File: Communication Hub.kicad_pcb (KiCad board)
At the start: 2 copper layers, 150 x 80 mm, 50 parts, among them J1 USB_B, J2 USB_A, J3 Conn_01x03, J4 Conn_01x02, J5 RJ45, J6 RJ45, J7 RJ45, U1 USBLC6-2SC6, U2 AT24CS02-SSHM, U3 USB2514B_Bi, U4 USBLC6-2SC6, U5 CP2102N-Axx-xQFN28, U6 MAX3485, Y1 24Mhz

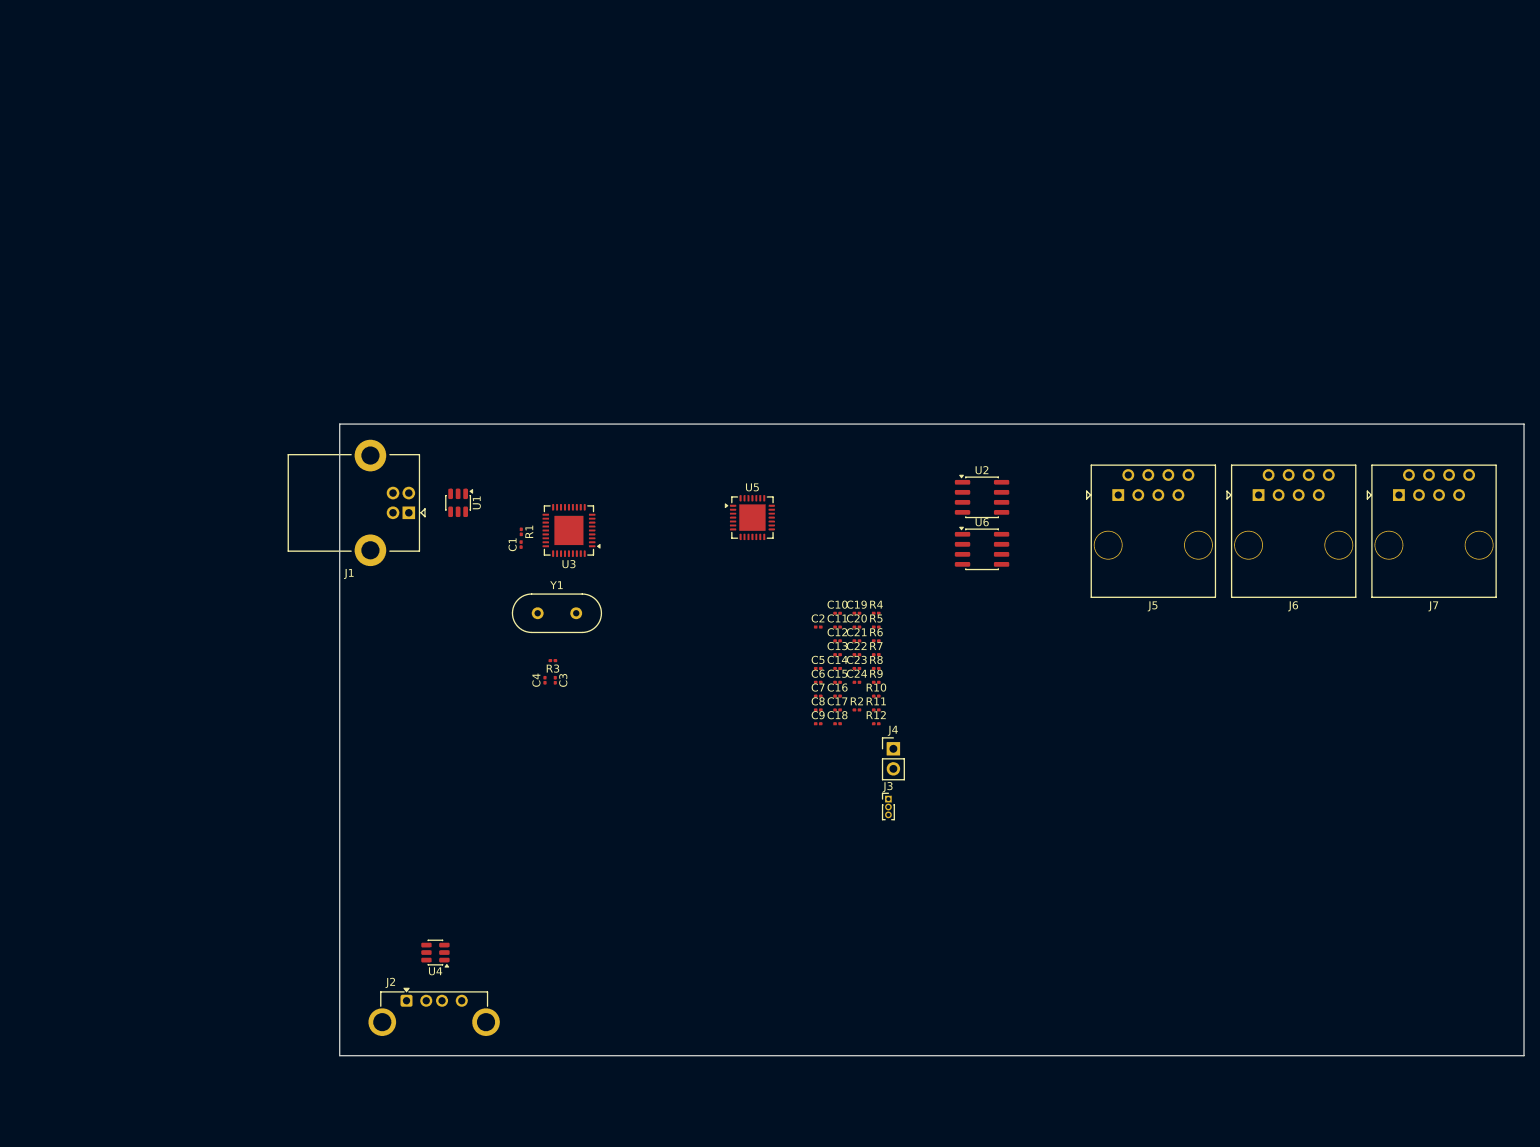
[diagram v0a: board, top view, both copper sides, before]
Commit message: Updates to schematics and pcb
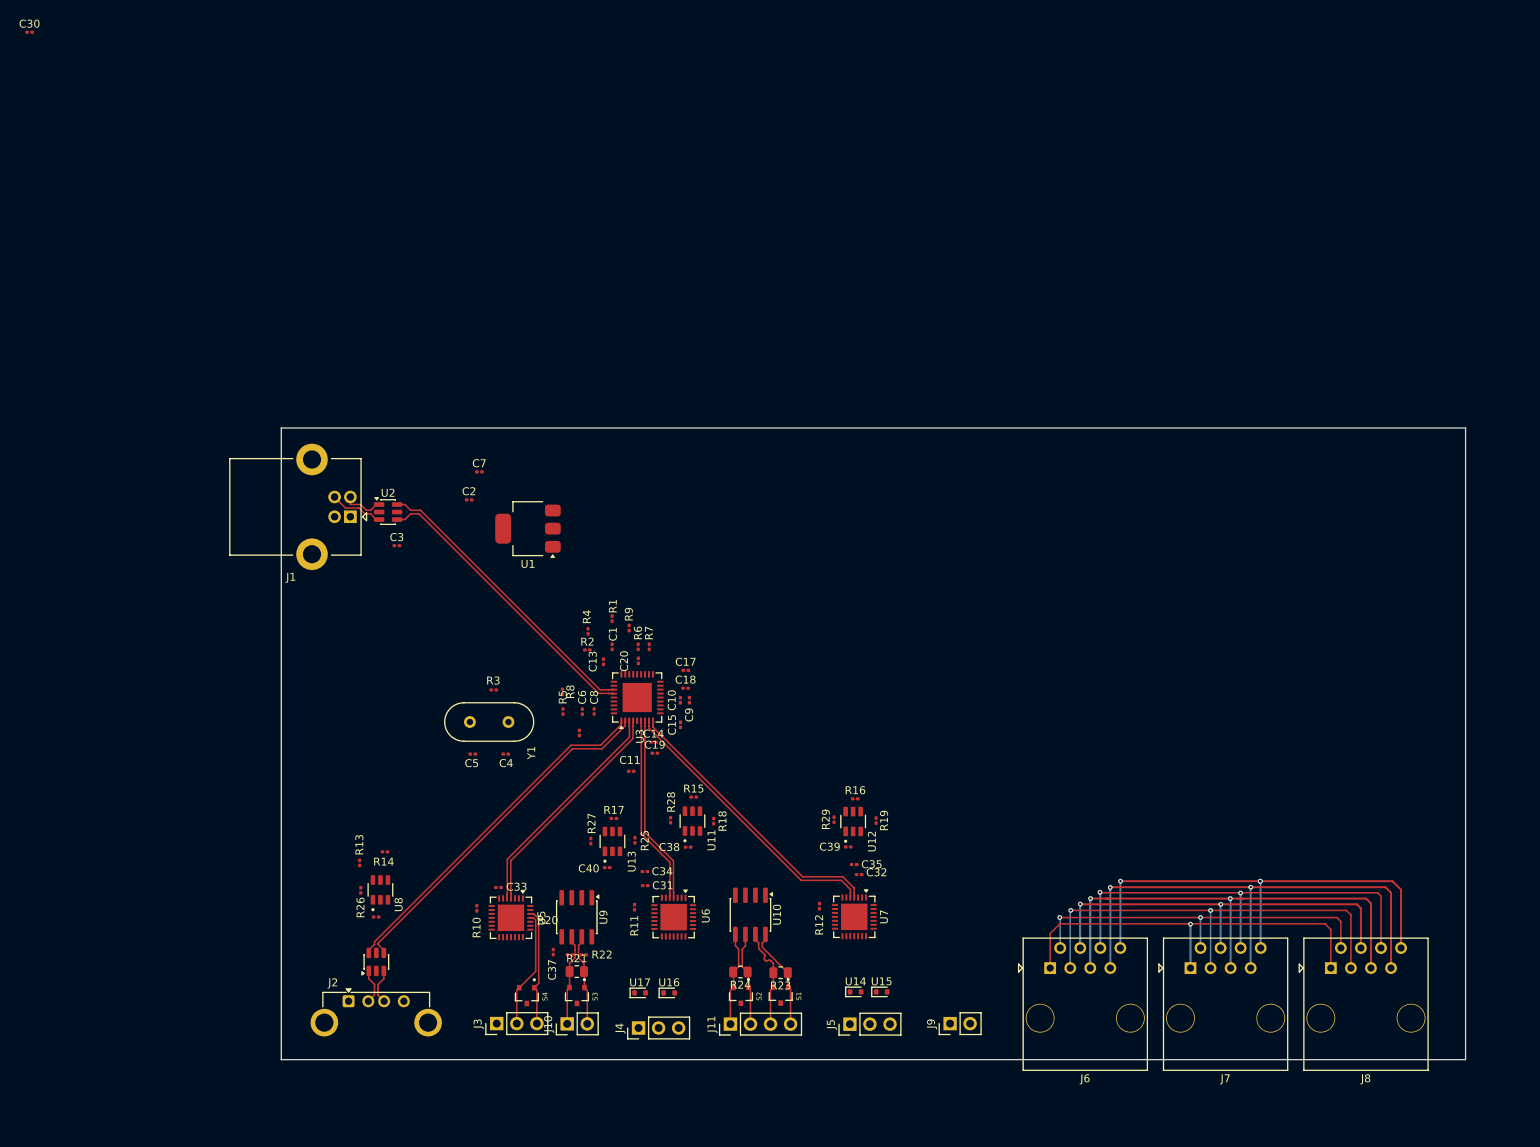
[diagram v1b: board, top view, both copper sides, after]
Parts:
- removed the C10 at (103.1, 74.0)
- removed the C19 at (105.5, 74.0)
- removed the C20 at (105.5, 75.7)
- removed C21, C22: 0,1uF, Capacitor_SMD:C_0201_0603Metric
- removed the R9 at (108.0, 82.7)
- removed the U2 at (121.4, 59.3)
- added C2: 10uF, Capacitor_SMD:C_0201_0603Metric, F.Cu at (56.4, 59.6)
- added C30: 0,1uF, Capacitor_SMD:C_0201_0603Metric, F.Cu at (0.72, 0.38)
- added C31: 0,1uF, Capacitor_SMD:C_0201_0603Metric, F.Cu at (78.7, 108.5)
- added C32: 0,1uF, Capacitor_SMD:C_0201_0603Metric, F.Cu at (105.8, 107.1)
- added C34: 4,7uF, Capacitor_SMD:C_0201_0603Metric, F.Cu at (78.7, 106.7)
- added C35: 4,7uF, Capacitor_SMD:C_0201_0603Metric, F.Cu at (105.2, 105.8)
- added C36: 0,1uF, Capacitor_SMD:C_0201_0603Metric, F.Cu at (44.6, 112.4)
- added C38: 0,1uF, Capacitor_SMD:C_0201_0603Metric, F.Cu at (84.1, 103.6)
- added C39: 0,1uF, Capacitor_SMD:C_0201_0603Metric, F.Cu at (104.4, 103.6)
- added C40: 0,1uF, Capacitor_SMD:C_0201_0603Metric, F.Cu at (73.9, 106.2)
- added C7: 22uF, Capacitor_SMD:C_0201_0603Metric, F.Cu at (57.7, 56.0)
- added J11: RS422, Connector_PinHeader_2.54mm:PinHeader_1x04_P2.54mm_Vertical, F.Cu at (89.5, 126.0)
- added J4: U6 TX RX, Connector_PinHeader_2.54mm:PinHeader_1x03_P2.54mm_Vertical, F.Cu at (77.9, 126.5)
- added J5: U7 TX RX, Connector_PinHeader_2.54mm:PinHeader_1x03_P2.54mm_Vertical, F.Cu at (104.6, 126.0)
- added J9: CAN, Connector_PinHeader_2.54mm:PinHeader_1x02_P2.54mm_Vertical, F.Cu at (117.3, 125.9)
- added R11: 10k, Resistor_SMD:R_0201_0603Metric, F.Cu at (77.3, 111.2)
- added R12: 10k, Resistor_SMD:R_0201_0603Metric, F.Cu at (100.8, 111.1)
- added R13: 49k, Resistor_SMD:R_0201_0603Metric, F.Cu at (42.5, 105.6)
- added R14: 100k, Resistor_SMD:R_0201_0603Metric, F.Cu at (45.7, 104.2)
- added R15: 235k, Resistor_SMD:R_0201_0603Metric, F.Cu at (84.8, 97.3)
- added R16: 235k, Resistor_SMD:R_0201_0603Metric, F.Cu at (105.3, 97.5)
- added R17: 235k, Resistor_SMD:R_0201_0603Metric, F.Cu at (74.7, 100.0)
- added R18: 100k, Resistor_SMD:R_0201_0603Metric, F.Cu at (87.4, 100.3)
- added R19: 100k, Resistor_SMD:R_0201_0603Metric, F.Cu at (107.9, 100.2)
- added R23: 120, Resistor_SMD:R_0805_2012Metric, F.Cu at (95.8, 119.5)
- added R24: `120, Resistor_SMD:R_0805_2012Metric, F.Cu at (90.8, 119.4)
- added R25: 100k, Resistor_SMD:R_0201_0603Metric, F.Cu at (77.4, 102.7)
- added R26: 0R, Resistor_SMD:R_0201_0603Metric, F.Cu at (42.7, 109.1)
- added R27: 0R, Resistor_SMD:R_0201_0603Metric, F.Cu at (71.8, 102.8)
- added R28: 0R, Resistor_SMD:R_0201_0603Metric, F.Cu at (81.9, 100.2)
- added R29: 0R, Resistor_SMD:R_0201_0603Metric, F.Cu at (102.6, 100.1)
- added R5: 12k, Resistor_SMD:R_0201_0603Metric, F.Cu at (68.3, 86.4)
- added R8: 100k, Resistor_SMD:R_0201_0603Metric, F.Cu at (68.2, 83.9)
- added S1: PESD2CAN_215, 1_My_custom_library:DIO_PESD2CAN_215, F.Cu at (95.9, 122.3)
- added S2: PESD2CAN_215, 1_My_custom_library:DIO_PESD2CAN_215, F.Cu at (90.8, 122.4)
- added S3: PESD2CAN_215, 1_My_custom_library:DIO_PESD2CAN_215, F.Cu at (70.0, 122.4)
- added S4: PESD2CAN_215, 1_My_custom_library:DIO_PESD2CAN_215, F.Cu at (63.7, 122.4)
- added U1: AMS1117-3.3, Package_TO_SOT_SMD:SOT-223-3_TabPin2, F.Cu at (63.9, 63.2)
- added U10: MAX490E, Package_SO:SOIC-8_3.9x4.9mm_P1.27mm, F.Cu at (92.0, 112.2)
- added U11: TPS2553DBVR, 1_My_custom_library:SOT95P280X145-6N, F.Cu at (84.7, 100.3)
- added U12: TPS2553DBVR, 1_My_custom_library:SOT95P280X145-6N, F.Cu at (105.0, 100.3)
- added U13: TPS2553DBVR, 1_My_custom_library:SOT95P280X145-6N, F.Cu at (74.5, 102.9)
- added U14: TPD1E05U06DYA, Diode_SMD:D_SOD-523, F.Cu at (105.3, 121.9)
- added U15: TPD1E05U06DYA, Diode_SMD:D_SOD-523, F.Cu at (108.6, 121.9)
- added U16: TPD1E05U06DYA, Diode_SMD:D_SOD-523, F.Cu at (81.7, 122.0)
- added U17: TPD1E05U06DYA, Diode_SMD:D_SOD-523, F.Cu at (78.0, 122.0)
- added U6: CP2102N-Axx-xQFN28, Package_DFN_QFN:QFN-28-1EP_5x5mm_P0.5mm_EP3.35x3.35mm, F.Cu at (82.3, 112.5)
- added U7: CP2102N-Axx-xQFN28, Package_DFN_QFN:QFN-28-1EP_5x5mm_P0.5mm_EP3.35x3.35mm, F.Cu at (105.2, 112.4)
- added U8: TPS2553DBVR, 1_My_custom_library:SOT95P280X145-6N, F.Cu at (45.2, 109.0)
- C10: renamed from C8; value `0,1uF -> 0,1uF
- C3: renamed from C2; value 1nF -> 1uF
- J10: renamed from J4; value Conn_01x02 -> RS485
- J3: value Conn_01x03 -> U5 TX RX; footprint Connector_PinHeader_1.00mm:PinHeader_1x03_P1.00mm_Vertical -> Connector_PinHeader_2.54mm:PinHeader_1x03_P2.54mm_Vertical
- R21: renamed from R11; footprint Resistor_SMD:R_0201_0603Metric -> Resistor_SMD:R_0805_2012Metric
- R6, R7: value 10k -> 100k
- moved U9 69.3 mm to (70.0, 112.5), turned to -90 degrees
- moved J6 60.5 mm to (130.0, 118.9)
- moved J7 60.5 mm to (147.8, 118.9)
- moved J8 60.5 mm to (165.5, 118.9)
- moved U5 59.2 mm to (61.7, 112.5), turned to -90 degrees
- moved R10 59.0 mm to (57.4, 111.3), turned to -90 degrees
- moved J3 57.2 mm to (59.9, 125.9), turned to 90 degrees
- moved C3 54.4 mm to (47.2, 65.4)
- moved J10 54.0 mm to (68.8, 126.0), turned to 90 degrees
- moved C33 53.2 mm to (60.1, 108.7), turned to 180 degrees
- moved C37 51.4 mm to (67.1, 116.9), turned to -90 degrees
- moved R20 50.8 mm to (69.2, 117.2)
- moved R21 50.4 mm to (70.0, 119.3)
- moved R22 47.2 mm to (70.9, 117.2)
- moved R4 36.6 mm to (71.5, 76.3), turned to 90 degrees
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- renumbered C9 to C11, C11 to C13, C12 to C14, C13 to C15, C14 to C16, C15 to C17, C16 to C18, C17 to C19, C18 to C20, C23 to C33, C24 to C37, C3 to C4, C4 to C5, C5 to C6, C6 to C8, C7 to C9, J5 to J6, J6 to J7, J7 to J8, R8 to R10, R10 to R20, R12 to R22, R5 to R9, U1 to U2, U6 to U9
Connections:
- net Net-(J3-Pin_2) renamed U5 RX
- net Net-(J4-Pin_1) renamed RS485+
- net Net-(J4-Pin_2) renamed RS485-
- net Net-(U3-USBDM_DN2/PRT_DIS_M2) renamed /USD2_DN
- net Net-(U3-USBDP_DN2/PRT_DIS_P2) renamed /USD2_DP
- C3 pad 1: Net-(J1-VBUS) -> +5V
- J1 pad 1: Net-(J1-VBUS) -> +5V
- J1 pad 2: Net-(J1-D-) -> /DN
- J1 pad 3: Net-(J1-D+) -> /DP
- J2 pad 1: Net-(J1-VBUS) -> Net-(J2-VBUS)
- J2 pad 2: Net-(J2-D-) -> /USBA_DN
- J2 pad 3: Net-(J2-D+) -> /USBA_DP
- J3 pad 1: Net-(J3-Pin_1) -> GND
- J3 pad 3: GND -> U5 TX
- J6 pad 1: unconnected-(J5-Pad1) -> RS485 A
- J6 pad 2: unconnected-(J5-Pad2) -> RS485 B
- J6 pad 3: unconnected-(J5-Pad3) -> RS422 A
- J6 pad 4: unconnected-(J5-Pad4) -> RS422 B
- J6 pad 5: unconnected-(J5-Pad5) -> RS422 Z
- J6 pad 6: unconnected-(J5-Pad6) -> RS422 Y
- J6 pad 7: unconnected-(J5-Pad7) -> CAN H
- J6 pad 8: unconnected-(J5-Pad8) -> CAN L
- J7 pad 1: unconnected-(J6-Pad1) -> RS485 A
- J7 pad 2: unconnected-(J6-Pad2) -> RS485 B
- J7 pad 3: unconnected-(J6-Pad3) -> RS422 A
- J7 pad 4: unconnected-(J6-Pad4) -> RS422 B
- J7 pad 5: unconnected-(J6-Pad5) -> RS422 Z
- J7 pad 6: unconnected-(J6-Pad6) -> RS422 Y
- J7 pad 7: unconnected-(J6-Pad7) -> CAN H
- J7 pad 8: unconnected-(J6-Pad8) -> CAN L
- J8 pad 1: unconnected-(J7-Pad1) -> RS485 A
- J8 pad 2: unconnected-(J7-Pad2) -> RS485 B
- J8 pad 3: unconnected-(J7-Pad3) -> RS422 A
- J8 pad 4: unconnected-(J7-Pad4) -> RS422 B
- J8 pad 5: unconnected-(J7-Pad5) -> RS422 Z
- J8 pad 6: unconnected-(J7-Pad6) -> RS422 Y
- J8 pad 7: unconnected-(J7-Pad7) -> CAN H
- J8 pad 8: unconnected-(J7-Pad8) -> CAN L
- R2 pad 1: Net-(J1-VBUS) -> +5V
- R6 pad 1: Net-(U2-SDA) -> GND
- R6 pad 2: +3.3V -> Net-(U3-SCL/SMBCLK/CFG_SEL0)
- R7 pad 1: Net-(U2-SCL) -> GND
- R7 pad 2: +3.3V -> Net-(U3-SDA/SMBDATA/NON_REM1)
- U2 pad 1: Net-(J1-D+) -> /DN
- U2 pad 2: GND -> +5V
- U2 pad 3: Net-(J1-D-) -> /DP
- U2 pad 4: Net-(U3-USBDM_UP) -> /DP
- U2 pad 5: Net-(J1-VBUS) -> GND
- U2 pad 6: Net-(U3-USBDP_UP) -> /DN
- U3 pad 1: Net-(U3-USBDM_DN1/PRT_DIS_M1) -> /USBA_DN
- U3 pad 12: unconnected-(U3-PRTPWR1/BC_EN1-Pad12) -> /PRTPWR1
- U3 pad 13: unconnected-(U3-OCS_N1-Pad13) -> /OCS_N1
- U3 pad 16: unconnected-(U3-PRTPWR2/BC_EN2-Pad16) -> /PRTPWR2
- U3 pad 17: unconnected-(U3-OCS_N2-Pad17) -> /OCS_N2
- U3 pad 18: unconnected-(U3-PRTPWR3/BC_EN3-Pad18) -> /PRTPWR3
- U3 pad 19: unconnected-(U3-OCS_N3-Pad19) -> /OCS_N3
- U3 pad 2: Net-(U3-USBDP_DN1/PRT_DIS_P1) -> /USBA_DP
- U3 pad 20: unconnected-(U3-PRTPWR4/BC_EN4-Pad20) -> /PRTPWR4
- U3 pad 21: unconnected-(U3-OCS_N4-Pad21) -> /OCS_N4
- U3 pad 22: Net-(U2-SDA) -> Net-(U3-SDA/SMBDATA/NON_REM1)
- U3 pad 24: Net-(U2-SCL) -> Net-(U3-SCL/SMBCLK/CFG_SEL0)
- U3 pad 28: unconnected-(U3-SUSP_IND/LOCAL_PWR/NON_REM0-Pad28) -> Net-(U3-SUSP_IND/LOCAL_PWR/NON_REM0)
- U3 pad 30: Net-(U3-USBDM_UP) -> /DN
- U3 pad 31: Net-(U3-USBDP_UP) -> /DP
- U3 pad 35: unconnected-(U3-RBIAS-Pad35) -> Net-(U3-RBIAS)
- U3 pad 6: unconnected-(U3-USBDM_DN3/PRT_DIS_M3-Pad6) -> /USD3_DN
- U3 pad 7: unconnected-(U3-USBDP_DN3/PRT_DIS_P3-Pad7) -> /USD3_DP
- U3 pad 8: unconnected-(U3-USBDM_DN4/PRT_DIS_M4-Pad8) -> /USD4_DN
- U3 pad 9: unconnected-(U3-USBDP_DN4/PRT_DIS_P4-Pad9) -> /USD4_DP
- U4 pad 1: Net-(J2-D+) -> /USBA_DN
- U4 pad 2: GND -> Net-(J2-VBUS)
- U4 pad 3: Net-(J2-D-) -> /USBA_DP
- U4 pad 4: Net-(U3-USBDM_DN1/PRT_DIS_M1) -> /USBA_DP
- U4 pad 5: Net-(J1-VBUS) -> GND
- U4 pad 6: Net-(U3-USBDP_DN1/PRT_DIS_P1) -> /USBA_DN
- U5 pad 17: unconnected-(U5-RS485/GPIO.2-Pad17) -> Net-(U5-RS485/GPIO.2)
- U5 pad 26: Net-(J3-Pin_1) -> U5 TX
- U5 pad 8: Net-(J1-VBUS) -> /VBUS2
- U9 pad 2: Net-(U6-DE) -> Net-(U5-RS485/GPIO.2)
- U9 pad 3: Net-(U6-DE) -> Net-(U5-RS485/GPIO.2)
- U9 pad 4: Net-(J3-Pin_1) -> U5 TX
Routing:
- net CAN H: track 0.00 -> 66.5 mm, vias 0 -> 2
- net RS422 Z: track 0.00 -> 61.9 mm, vias 0 -> 2
- net CAN L: track 0.00 -> 60.3 mm, vias 0 -> 3
- net RS422 A: track 0.00 -> 57.5 mm, vias 0 -> 2
- net RS422 Y: track 0.00 -> 57.1 mm, vias 0 -> 2
- net RS422 B: track 0.00 -> 51.9 mm, vias 0 -> 2
- net RS485 A: track 0.00 -> 51.2 mm, vias 0 -> 1
- net /USBA_DN: track 0.00 -> 49.4 mm
- net /USBA_DP: track 0.00 -> 49.4 mm
- net RS485 B: track 0.00 -> 46.9 mm, vias 0 -> 2
- net /DP: track 0.00 -> 44.3 mm
- net /DN: track 0.00 -> 42.7 mm
- net /USD4_DP: track 0.00 -> 36.0 mm
- net /USD4_DN: track 0.00 -> 36.0 mm
- net /USD2_DP: track 0.00 -> 28.9 mm
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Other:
- copper layers 2 -> 4

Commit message: major update to pcb and corrections to schematics
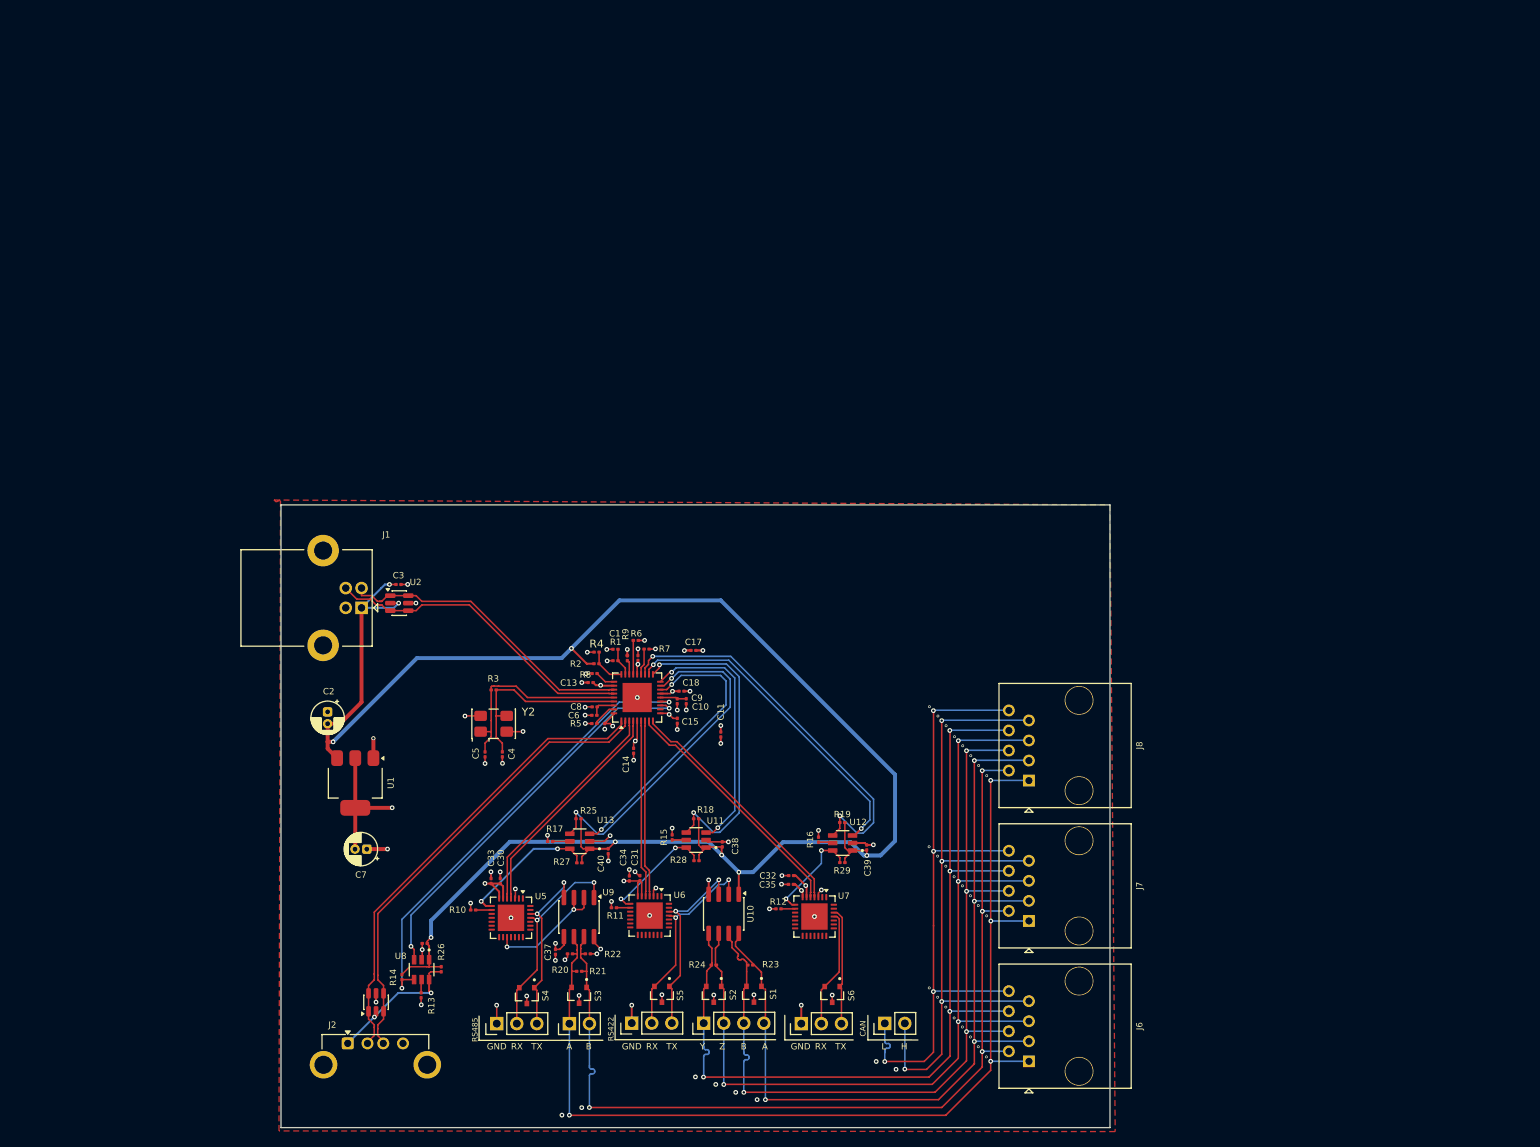
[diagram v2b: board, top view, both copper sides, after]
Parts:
- removed C19: 0,1uF, Capacitor_SMD:C_0201_0603Metric
- removed U14, U15, U16, U17: TPD1E05U06DYA, Diode_SMD:D_SOD-523
- removed Y1: 24Mhz, Crystal:Crystal_HC49-4H_Vertical
- added S5: PESD2CAN_215, 1_My_custom_library:DIO_PESD2CAN_215, F.Cu at (80.8, 122.2)
- added S6: PESD2CAN_215, 1_My_custom_library:DIO_PESD2CAN_215, F.Cu at (102.4, 122.2)
- added Y2: 24Mhz, Crystal:Crystal_SMD_5032-4Pin_5.0x3.2mm, F.Cu at (59.5, 88.0)
- C2, C7: footprint Capacitor_SMD:C_0201_0603Metric -> Capacitor_THT:CP_Radial_D4.0mm_P1.50mm
- R21, R23, R24: footprint Resistor_SMD:R_0805_2012Metric -> Resistor_SMD:R_0201_0603Metric
- moved C30 122.9 mm to (60.3, 107.9), turned to -90 degrees
- moved C7 49.9 mm to (43.4, 103.8), turned to 180 degrees
- moved J8 45.0 mm to (127.3, 95.2), turned to 90 degrees
- moved U1 38.9 mm to (42.0, 95.5), turned to -90 degrees
- moved C2 32.3 mm to (38.5, 86.5), turned to -90 degrees
- moved J7 21.3 mm to (127.3, 112.9), turned to 90 degrees
- moved R13 18.5 mm to (50.3, 122.3)
- moved R14 16.0 mm to (47.9, 120.0), turned to 90 degrees
- moved R26 14.3 mm to (52.9, 119.1), turned to 90 degrees
- moved C11 12.3 mm to (88.3, 89.3), turned to 90 degrees
- moved J6 12.1 mm to (127.3, 130.7), turned to 90 degrees
- moved J1 11.6 mm to (42.8, 73.3)
- moved U2 11.6 mm to (47.5, 72.7)
- moved U8 11.4 mm to (50.4, 119.1), turned to -90 degrees
- moved C32 8.61 mm to (97.2, 107.2), turned to 0 degrees
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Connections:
- net +5V renamed VBUS
- J4 pad 1: U6 TX -> GND
- J4 pad 3: GND -> U6 TX
- J6 pad 1: RS485 A -> RS485+
- J6 pad 2: RS485 B -> RS485-
- J6 pad 3: RS422 A -> RS422 AB_P
- J6 pad 4: RS422 B -> RS422 AB_N
- J6 pad 5: RS422 Z -> RS422 ZY_N
- J6 pad 6: RS422 Y -> RS422 ZY_P
- J7 pad 1: RS485 A -> RS485+
- J7 pad 2: RS485 B -> RS485-
- J7 pad 3: RS422 A -> RS422 AB_P
- J7 pad 4: RS422 B -> RS422 AB_N
- J7 pad 5: RS422 Z -> RS422 ZY_N
- J7 pad 6: RS422 Y -> RS422 ZY_P
- J8 pad 1: RS485 A -> RS485+
- J8 pad 2: RS485 B -> RS485-
- J8 pad 3: RS422 A -> RS422 AB_P
- J8 pad 4: RS422 B -> RS422 AB_N
- J8 pad 5: RS422 Z -> RS422 ZY_N
- J8 pad 6: RS422 Y -> RS422 ZY_P
- R4 pad 1: Net-(U3-VBUS_DET) -> GND
- R4 pad 2: GND -> Net-(U3-VBUS_DET)
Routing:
- net VBUS: track 0.00 -> 245.4 mm, vias 0 -> 9
- net RS485+: track 12.3 -> 132.1 mm, vias 0 -> 4
- net RS485-: track 12.3 -> 124.7 mm, vias 0 -> 4
- net RS422 ZY_N: track 12.1 -> 117.9 mm, vias 0 -> 4
- net RS422 ZY_P: track 12.2 -> 115.8 mm, vias 0 -> 4
- net RS422 AB_P: track 13.0 -> 110.2 mm, vias 0 -> 4
- net RS422 AB_N: track 12.9 -> 107.9 mm, vias 0 -> 4
- net GND: track 0.00 -> 72.6 mm, vias 0 -> 93
- net RS422 Z: track 61.9 -> 0.00 mm, vias 2 -> 0
- net +3.3V: track 0.00 -> 60.0 mm, vias 0 -> 21
- net /OCS_N1: track 0.00 -> 57.7 mm, vias 0 -> 2
- net RS422 A: track 57.5 -> 0.00 mm, vias 2 -> 0
- net RS422 Y: track 57.1 -> 0.00 mm, vias 2 -> 0
- net RS422 B: track 51.9 -> 0.00 mm, vias 2 -> 0
- net RS485 A: track 51.2 -> 0.00 mm, vias 1 -> 0
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- added copper zone on In2.Cu, net +3.3V
- added copper zone on F.Cu, net GND
- added copper zone on In1.Cu, net GND
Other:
- board size 150 x 80 mm -> 105 x 78.9 mm
- board text added: "A"
- board text added: "B"
- board text added: "CAN"
- board text added: "GND"
- board text added: "H"
- board text added: "L"
- board text added: "RS422"
- board text added: "RS485"
- board text added: "RX"
- board text added: "TX"
- board text added: "Y"
- board text added: "Z"

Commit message: Corrections to PCB
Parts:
- moved C36 2.87 mm to (50.7, 118.7)
- moved J2 2.87 mm to (41.0, 131.3)
- moved R13 2.87 mm to (50.3, 125.2)
- moved R14 2.87 mm to (47.8, 122.9)
- moved R26 2.87 mm to (52.8, 121.9)
- moved U4 2.87 mm to (44.6, 126.1)
- moved U8 2.87 mm to (50.3, 122.0)
- moved C32 1.10 mm to (96.3, 107.8)
- moved C35 1.10 mm to (96.3, 108.9)
- moved C30 0.32 mm to (60.0, 107.9)
- moved R8 0.24 mm to (72.3, 81.4)
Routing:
- net /USBA_DN: track 59.3 -> 62.6 mm
- net /USBA_DP: track 59.4 -> 62.6 mm
- net /OCS_N1: track 57.7 -> 60.9 mm
- net /PRTPWR1: track 50.7 -> 53.6 mm
- net VBUS: track 245.4 -> 248.3 mm
- net /USD4_DN: track 31.6 -> 30.9 mm
- net /USD4_DP: track 31.7 -> 30.9 mm
- net +3.3V: track 60.0 -> 59.2 mm, vias 21 -> 20
- net GND: track 72.6 -> 73.2 mm
- net /DP: track 40.7 -> 41.2 mm
